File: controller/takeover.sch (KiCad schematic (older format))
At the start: 0 parts

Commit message: Start putting the controller together, add various subsystems
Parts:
- added C1, C10, C11, C12, C13, C14, C16, C2, C3, C4, C5, C6, C8, C9, C? (x2): C, symbol C
- added C15, C7: CP, symbol CP
- added D1, D10, D11, D12, D2, D3, D4, D5, D6, D7, D8, D9, D? (x2): D_ALT, symbol D_ALT
- added J1, J10, J11, J12, J13, J2, J3, J4, J5, J6, J7, J8, J9, J? (x3): CONN_01X02, symbol CONN_01X02
- added K1, K10, K11, K12, K13, K14, K2, K3, K4, K5, K6, K7, K8, K9: RELAY_SEPARATED, symbol RELAY_SEPARATED
- added R1, R2: R, symbol R
- added U1, U2: ULN2003, symbol ULN2003
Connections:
- net labels added: +5V, COMMON_OUT, COMMON_REAL, DIR_SW_BACK_HACK, DIR_SW_BACK_OUT, DIR_SW_BACK_REAL, DIR_SW_FWD_HACK, DIR_SW_FWD_OUT, DIR_SW_FWD_REAL, GAZ_POT_GND_HACK, GAZ_POT_GND_OUT, GAZ_POT_GND_REAL, GAZ_POT_V_HACK, GAZ_POT_V_OUT, GAZ_POT_V_REAL, GAZ_POT_WIPER_HACK, GAZ_POT_WIPER_OUT, GAZ_POT_WIPER_REAL, GAZ_SW_COMMON, GAZ_SW_COMMON_OUT, GAZ_SW_COMMON_REAL, GAZ_SW_NC_HACK, GAZ_SW_NC_OUT, GAZ_SW_NC_REAL, GAZ_SW_NO_HACK, GAZ_SW_NO_OUT, GAZ_SW_NO_REAL, GND, HORN_SW_HACK, HORN_SW_OUT, HORN_SW_REAL, PARKING_HACK, PARKING_OUT, PARKING_REAL, STEERING_COMMON, VCC
- wire segments 0 -> 200
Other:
- note added: "TODO: MIRGALKĖ"
- note added: "TODO: RAKTELIS"
- note added: "TODO: SĖDYNĖ"
- note added: "TODO: ŠVIESOS"

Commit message: Add more stuff to controller, start sourcing parts
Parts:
- removed J1, J10, J11, J12, J13, J2, J3, J4, J5, J6, J7, J8, J9, J? (x3): CONN_01X02, symbol CONN_01X02
- removed U1, U2: ULN2003, symbol ULN2003
- added C19, C32: C, Capacitors_SMD:C_0603_HandSoldering, symbol C
- added D15, D27: D_ALT, Diodes_SMD:D_SOD-123, symbol D_ALT
- added D28, D29: 16V, symbol D_Zener
- added J? (x4): CONN_01X10, Connectors_Terminal_Blocks:TerminalBlock_Pheonix_MKDS1.5-10pol, symbol CONN_01X10
- added K15: RELAY_SEPARATED, smalsiukas-footpints:Relay_SPDT, symbol RELAY_SEPARATED
- added K16: RELAY_SEPARATED, symbol RELAY_SEPARATED
- added U2, U6: ULN2801A, Housings_SOIC:SOIC-18W_7.5x11.6mm_Pitch1.27mm, symbol ULN2801A
- C1, C10, C11, C12, C13, C14, C2, C3, C4, C5, C6, C9: footprint (none) -> Capacitors_SMD:C_0603_HandSoldering; Distributor (none) -> ?; Manufacturer (none) -> ?; PartNo (none) -> ?
- C17, C18: renamed from C?; footprint (none) -> Capacitors_SMD:C_0603_HandSoldering; Distributor (none) -> ?; Manufacturer (none) -> ?; PartNo (none) -> ?
- D1: footprint (none) -> Diodes_SMD:D_SOD-123; Distributor (none) -> 1510679; Manufacturer (none) -> ?; PartNo (none) -> PMEG2020EH
- D10, D11, D12, D2, D3, D4, D5, D6, D7, D8, D9: footprint (none) -> Diodes_SMD:D_SOD-123; Distributor (none) -> ?; Manufacturer (none) -> ?; PartNo (none) -> ?
- D13, D14: renamed from D?; footprint (none) -> Diodes_SMD:D_SOD-123; Distributor (none) -> ?; Manufacturer (none) -> ?; PartNo (none) -> ?
- K1, K10, K11, K12, K13, K14, K2, K3, K4, K5, K6, K7, K8, K9: footprint (none) -> smalsiukas-footpints:Relay_SPDT
- renumbered R1 to R91, R2 to R92
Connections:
- net labels added: AUX_COMMON, AUX_COMMON_OUT, AUX_COMMON_REAL, AUX_HACK, AUX_OUT, AUX_REAL, KEY_COLD_HACK, KEY_COLD_OUT, KEY_COLD_REAL, KEY_HOT_HACK, KEY_HOT_OUT, KEY_HOT_REAL, LIGHTS_COMMON, LIGHTS_COMMON_OUT, LIGHTS_COMMON_REAL, LIGHTS_HACK, LIGHTS_OUT, LIGHTS_REAL, MIRGALKE_HACK, MIRGALKE_OUT, MIRGALKE_REAL, SEAT_GND_HACK, SEAT_GND_OUT, SEAT_GND_REAL, SEAT_HACK, SEAT_OUT, SEAT_REAL, TAKEOVER
- net labels removed: +5V
- wire segments 200 -> 306
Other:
- note removed: "TODO: MIRGALKĖ"
- note removed: "TODO: RAKTELIS"
- note removed: "TODO: SĖDYNĖ"
- note removed: "TODO: ŠVIESOS"
- moved on the sheet: C16, K10A, K10B, K11A, K11B, K12A, K12B, K13A, K13B, K14A, K14B, K7B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

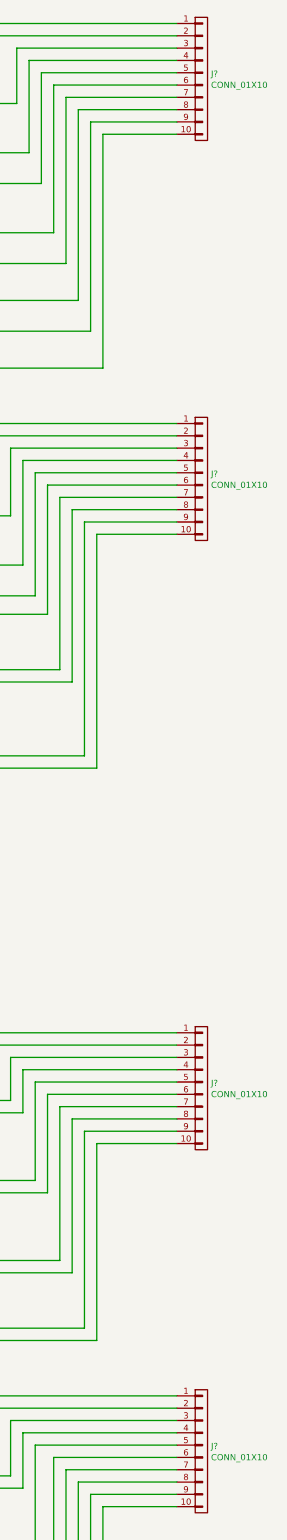
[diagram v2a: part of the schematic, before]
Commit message: Change gas pedal interface so that it supports going up and down from the middle voltage so that it's compatible with Linde forklift gas mechanism
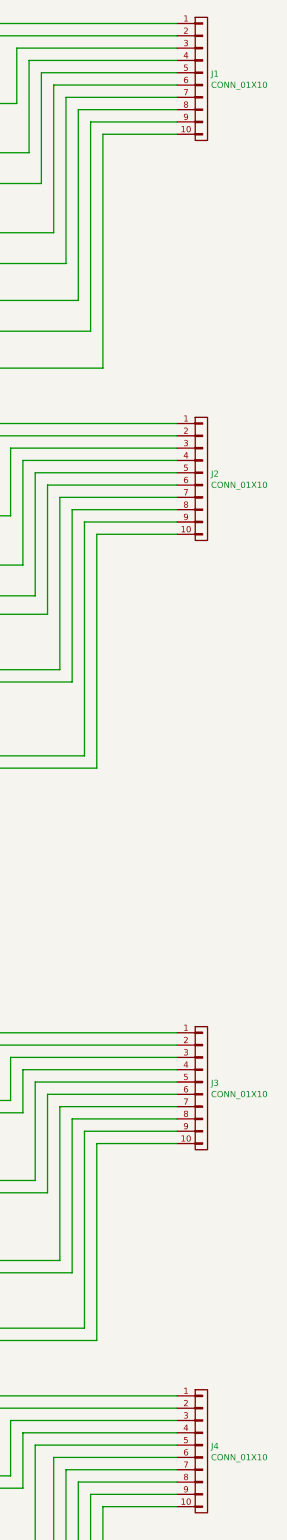
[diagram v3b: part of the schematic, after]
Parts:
- C16: footprint (none) -> Capacitors_SMD:C_0603_HandSoldering
- K1, K10, K11, K12, K13, K14, K15, K16, K2, K3, K4, K5, K6, K7, K8, K9: footprint (none) -> smalsiukas-footpints:Relay_SPDT
- R91, R92: footprint (none) -> Resistors_SMD:R_0603_HandSoldering
- gave numbers to parts that had none: 4
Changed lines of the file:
@@
 F 0 "K2" V 13100 2150 50  0000 C CNN
 F 1 "RELAY_SEPARATED" V 13537 2150 50  0001 C CNN
-F 2 "" H 8700 -250 50  0000 C CNN
+F 2 "smalsiukas-footpints:Relay_SPDT" H 8700 -250 50  0001 C CNN
 F 3 "" H 8700 -250 50  0000 C CNN
 F 4 "?" H 13350 2150 60  0001 C CNN "PartNo"
@@
 F 0 "K9" V 13100 9650 50  0000 C CNN
 F 1 "RELAY_SEPARATED" V 13200 9600 50  0001 C CNN
-F 2 "" H 8700 7200 50  0000 C CNN
+F 2 "smalsiukas-footpints:Relay_SPDT" H 8700 7200 50  0001 C CNN
 F 3 "" H 8700 7200 50  0000 C CNN
 F 4 "?" H 13350 9600 60  0001 C CNN "PartNo"
@@
 F 0 "K3" V 13150 2800 50  0000 C CNN
 F 1 "RELAY_SEPARATED" V 13537 2800 50  0001 C CNN
-F 2 "" H 8700 400 50  0000 C CNN
+F 2 "smalsiukas-footpints:Relay_SPDT" H 8700 400 50  0001 C CNN
 F 3 "" H 8700 400 50  0000 C CNN
 F 4 "?" H 13350 2800 60  0001 C CNN "PartNo"
@@
 F 0 "K10" V 13150 10250 50  0000 C CNN
 F 1 "RELAY_SEPARATED" V 13150 10250 50  0001 C CNN
-F 2 "" H 8700 7850 50  0000 C CNN
+F 2 "smalsiukas-footpints:Relay_SPDT" H 8700 7850 50  0001 C CNN
 F 3 "" H 8700 7850 50  0000 C CNN
 F 4 "?" H 13350 10250 60  0001 C CNN "PartNo"
@@
 F 0 "K1" V 13150 1500 50  0000 C CNN
 F 1 "RELAY_SEPARATED" V 13116 1500 50  0001 C CNN
-F 2 "" H 8700 -900 50  0000 C CNN
+F 2 "smalsiukas-footpints:Relay_SPDT" H 8700 -900 50  0001 C CNN
 F 3 "" H 8700 -900 50  0000 C CNN
 F 4 "?" H 13350 1500 60  0001 C CNN "PartNo"
@@
 F 0 "K8" V 13025 6800 50  0000 C CNN
 F 1 "RELAY_SEPARATED" V 13116 6800 50  0001 C CNN
-F 2 "" H 8700 4400 50  0000 C CNN
+F 2 "smalsiukas-footpints:Relay_SPDT" H 8700 4400 50  0001 C CNN
 F 3 "" H 8700 4400 50  0000 C CNN
 F 4 "?" H 13350 6800 60  0001 C CNN "PartNo"
@@
 $EndComp
 $Comp
-L GND #PWR01
+L GND #PWR1
 U 1 1 58C02975
 P 2100 3850
-F 0 "#PWR01" H -2250 300 50  0001 C CNN
+F 0 "#PWR1" H -2250 300 50  0001 C CNN
 F 1 "GND" H 2105 3677 50  0000 C CNN
 F 2 "" H -2250 550 50  0001 C CNN
@@
 F 0 "R91" H 1569 3746 50  0000 L CNN
 F 1 "R" H 1569 3655 50  0000 L CNN
-F 2 "" V -2120 1200 50  0001 C CNN
+F 2 "Resistors_SMD:R_0603_HandSoldering" V -2120 1200 50  0001 C CNN
 F 3 "" H -2050 1200 50  0001 C CNN
 	1    1500 3700
@@
 $EndComp
 $Comp
-L GND #PWR02
+L GND #PWR2
 U 1 1 58C02979
 P 4400 2700
-F 0 "#PWR02" H 50  -850 50  0001 C CNN
+F 0 "#PWR2" H 50  -850 50  0001 C CNN
 F 1 "GND" H 4405 2527 50  0000 C CNN
 F 2 "" H 50  -600 50  0001 C CNN
@@
 F 0 "K5" V 13550 4100 50  0000 C CNN
 F 1 "RELAY_SEPARATED" V 13537 4100 50  0001 C CNN
-F 2 "" H 8700 1700 50  0000 C CNN
+F 2 "smalsiukas-footpints:Relay_SPDT" H 8700 1700 50  0001 C CNN
 F 3 "" H 8700 1700 50  0000 C CNN
 F 4 "?" H 13350 4100 60  0001 C CNN "PartNo"
@@
 F 0 "K12" V 13150 11450 50  0000 C CNN
 F 1 "RELAY_SEPARATED" V 13200 11450 50  0001 C CNN
-F 2 "" H 8700 9050 50  0000 C CNN
+F 2 "smalsiukas-footpints:Relay_SPDT" H 8700 9050 50  0001 C CNN
 F 3 "" H 8700 9050 50  0000 C CNN
 F 4 "?" H 13350 11450 60  0001 C CNN "PartNo"
@@
 F 0 "K6" V 13150 4850 50  0000 C CNN
 F 1 "RELAY_SEPARATED" V 13537 4850 50  0001 C CNN
-F 2 "" H 8700 2450 50  0000 C CNN
+F 2 "smalsiukas-footpints:Relay_SPDT" H 8700 2450 50  0001 C CNN
 F 3 "" H 8700 2450 50  0000 C CNN
 F 4 "?" H 13350 4850 60  0001 C CNN "PartNo"
@@
 F 0 "K13" V 13050 12000 50  0000 C CNN
 F 1 "RELAY_SEPARATED" V 13150 12000 50  0001 C CNN
-F 2 "" H 8700 9600 50  0000 C CNN
+F 2 "smalsiukas-footpints:Relay_SPDT" H 8700 9600 50  0001 C CNN
 F 3 "" H 8700 9600 50  0000 C CNN
 F 4 "?" H 13350 12000 60  0001 C CNN "PartNo"
@@
 F 0 "K4" V 13150 3350 50  0000 C CNN
 F 1 "RELAY_SEPARATED" V 13116 3350 50  0001 C CNN
-F 2 "" H 8700 950 50  0000 C CNN
+F 2 "smalsiukas-footpints:Relay_SPDT" H 8700 950 50  0001 C CNN
 F 3 "" H 8700 950 50  0000 C CNN
 F 4 "?" H 13350 3350 60  0001 C CNN "PartNo"
@@
 F 0 "K11" V 13150 10900 50  0000 C CNN
 F 1 "RELAY_SEPARATED" V 13116 10900 50  0001 C CNN
-F 2 "" H 8700 8500 50  0000 C CNN
+F 2 "smalsiukas-footpints:Relay_SPDT" H 8700 8500 50  0001 C CNN
 F 3 "" H 8700 8500 50  0000 C CNN
 F 4 "?" H 13350 10900 60  0001 C CNN "PartNo"
@@
 $EndComp
 $Comp
-L GND #PWR03
+L GND #PWR4
 U 1 1 58C03628
 P 6550 3750
-F 0 "#PWR03" H 2200 200 50  0001 C CNN
+F 0 "#PWR4" H 2200 200 50  0001 C CNN
 F 1 "GND" H 6555 3577 50  0000 C CNN
 F 2 "" H 2200 450 50  0001 C CNN
@@
 F 0 "R92" H 6019 3646 50  0000 L CNN
 F 1 "R" H 6019 3555 50  0000 L CNN
-F 2 "" V 2330 1100 50  0001 C CNN
+F 2 "Resistors_SMD:R_0603_HandSoldering" V 2330 1100 50  0001 C CNN
 F 3 "" H 2400 1100 50  0001 C CNN
 	1    5950 3600
@@
 $EndComp
 $Comp
-L GND #PWR04
+L GND #PWR5
 U 1 1 58C0362C
 P 8850 2600
-F 0 "#PWR04" H 4500 -950 50  0001 C CNN
+F 0 "#PWR5" H 4500 -950 50  0001 C CNN
 F 1 "GND" H 8855 2427 50  0000 C CNN
 F 2 "" H 4500 -700 50  0001 C CNN
@@
 F 0 "C16" H 9085 2404 50  0000 R CNN
 F 1 "C" H 9085 2495 50  0000 R CNN
-F 2 "" H 1088 -3400 50  0001 C CNN
+F 2 "Capacitors_SMD:C_0603_HandSoldering" H 1088 -3400 50  0001 C CNN
 F 3 "" H 1050 -3250 50  0001 C CNN
 	1    9200 2450
@@
 F 0 "K7" V 13150 6100 50  0000 C CNN
 F 1 "RELAY_SEPARATED" V 13537 6100 50  0001 C CNN
-F 2 "" H 8700 3700 50  0000 C CNN
+F 2 "smalsiukas-footpints:Relay_SPDT" H 8700 3700 50  0001 C CNN
 F 3 "" H 8700 3700 50  0000 C CNN
 F 4 "?" H 13350 6100 60  0001 C CNN "PartNo"
@@
 F 0 "K14" V 13050 12650 50  0000 C CNN
 F 1 "RELAY_SEPARATED" V 13150 12650 50  0000 C CNN
-F 2 "" H 8700 10250 50  0000 C CNN
+F 2 "smalsiukas-footpints:Relay_SPDT" H 8700 10250 50  0001 C CNN
 F 3 "" H 8700 10250 50  0000 C CNN
 F 4 "?" H 13350 12650 60  0001 C CNN "PartNo"
@@
 F 0 "K16" V 13100 14150 50  0000 C CNN
 F 1 "RELAY_SEPARATED" V 13487 14150 50  0001 C CNN
-F 2 "" H 8650 11750 50  0000 C CNN
+F 2 "smalsiukas-footpints:Relay_SPDT" H 8650 11750 50  0001 C CNN
 F 3 "" H 8650 11750 50  0000 C CNN
 F 4 "?" H 13300 14150 60  0001 C CNN "PartNo"
@@
 F 0 "K15" V 13050 13400 50  0000 C CNN
 F 1 "RELAY_SEPARATED" V 13150 13400 50  0000 C CNN
-F 2 "" H 8700 11000 50  0000 C CNN
+F 2 "smalsiukas-footpints:Relay_SPDT" H 8700 11000 50  0001 C CNN
 F 3 "" H 8700 11000 50  0000 C CNN
 F 4 "?" H 13350 13400 60  0001 C CNN "PartNo"
@@
 $EndComp
 $Comp
-L GND #PWR05
+L GND #PWR3
 U 1 1 58D4FA8B
 P 5150 2700
-F 0 "#PWR05" H 800 -850 50  0001 C CNN
+F 0 "#PWR3" H 800 -850 50  0001 C CNN
 F 1 "GND" H 5155 2527 50  0000 C CNN
 F 2 "" H 800 -600 50  0001 C CNN
@@
 $EndComp
 $Comp
-L GND #PWR06
+L GND #PWR6
 U 1 1 58D50C69
 P 9550 2600
-F 0 "#PWR06" H 5200 -950 50  0001 C CNN
+F 0 "#PWR6" H 5200 -950 50  0001 C CNN
 F 1 "GND" H 9555 2427 50  0000 C CNN
 F 2 "" H 5200 -700 50  0001 C CNN
@@
 $EndComp
 $Comp
-L CONN_01X10 J?
+L CONN_01X10 J1
 U 1 1 58C69E7E
 P 16350 1300
-F 0 "J?" H 16428 1341 50  0000 L CNN
+F 0 "J1" H 16428 1341 50  0000 L CNN
 F 1 "CONN_01X10" H 16428 1250 50  0000 L CNN
 F 2 "Connectors_Terminal_Blocks:TerminalBlock_Pheonix_MKDS1.5-10pol" H -3750 -200 50  0001 C CNN
@@
 $EndComp
 $Comp
-L CONN_01X10 J?
+L CONN_01X10 J2
 U 1 1 58C75771
 P 16350 4550
-F 0 "J?" H 16428 4591 50  0000 L CNN
+F 0 "J2" H 16428 4591 50  0000 L CNN
 F 1 "CONN_01X10" H 16428 4500 50  0000 L CNN
 F 2 "Connectors_Terminal_Blocks:TerminalBlock_Pheonix_MKDS1.5-10pol" H -3750 3050 50  0001 C CNN
@@
 $EndComp
 $Comp
-L CONN_01X10 J?
+L CONN_01X10 J3
 U 1 1 58C75B19
 P 16350 9500
-F 0 "J?" H 16428 9541 50  0000 L CNN
+F 0 "J3" H 16428 9541 50  0000 L CNN
 F 1 "CONN_01X10" H 16428 9450 50  0000 L CNN
 F 2 "Connectors_Terminal_Blocks:TerminalBlock_Pheonix_MKDS1.5-10pol" H -3750 8000 50  0001 C CNN
@@
 $EndComp
 $Comp
-L CONN_01X10 J?
+L CONN_01X10 J4
 U 1 1 58C76546
 P 16350 12450
-F 0 "J?" H 16428 12491 50  0000 L CNN
+F 0 "J4" H 16428 12491 50  0000 L CNN
 F 1 "CONN_01X10" H 16428 12400 50  0000 L CNN
 F 2 "Connectors_Terminal_Blocks:TerminalBlock_Pheonix_MKDS1.5-10pol" H -3750 10950 50  0001 C CNN

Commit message: More or less final controller board
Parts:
- removed C15, C7: CP, symbol CP
- added C15, C7: 470u, Capacitors_ThroughHole:CP_Radial_D16.0mm_P7.50mm, symbol CP1
- C16: footprint Capacitors_SMD:C_0603_HandSoldering -> Capacitors_SMD:C_1210_HandSoldering; Distributor (none) -> ?; Manufacturer (none) -> ?; PartNo (none) -> ?
- C8: footprint (none) -> Capacitors_SMD:C_1210_HandSoldering; Distributor (none) -> ?; Manufacturer (none) -> ?; PartNo (none) -> ?
- D28, D29: footprint (none) -> Diodes_SMD:D_SMB_Handsoldering; Distributor (none) -> 1431172; Manufacturer (none) -> ON SEMI; PartNo (none) -> 1SMB5930BT3G
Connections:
- net GND: now also C15.2, C7.2
- net VCC: now also C15.1, C7.1
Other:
- note added: "Relės: HFD23/012-1ZS @ TME.eu\nhttp://www.tme.eu/en/details/hfd23_012-1zs/miniature-electromagnetic-relays/hongfa-relay/"
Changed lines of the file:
@@
 LIBS:valves
 LIBS:mic-parts
+LIBS:shield_arduino
 LIBS:controller-cache
 EELAYER 26 0
@@
 $EndComp
 $Comp
-L GND #PWR1
+L GND #PWR03
 U 1 1 58C02975
 P 2100 3850
-F 0 "#PWR1" H -2250 300 50  0001 C CNN
+F 0 "#PWR03" H -2250 300 50  0001 C CNN
 F 1 "GND" H 2105 3677 50  0000 C CNN
 F 2 "" H -2250 550 50  0001 C CNN
@@
 $EndComp
 $Comp
-L CP C7
-U 1 1 58C02978
-P 4400 2550
-F 0 "C7" H 4518 2596 50  0000 L CNN
-F 1 "CP" H 4518 2505 50  0000 L CNN
-F 2 "" H -2662 750 50  0001 C CNN
-F 3 "" H -2700 900 50  0001 C CNN
-	1    4400 2550
-	1    0    0    -1
-$EndComp
-$Comp
-L GND #PWR2
+L GND #PWR04
 U 1 1 58C02979
 P 4400 2700
-F 0 "#PWR2" H 50  -850 50  0001 C CNN
+F 0 "#PWR04" H 50  -850 50  0001 C CNN
 F 1 "GND" H 4405 2527 50  0000 C CNN
 F 2 "" H 50  -600 50  0001 C CNN
@@
 F 0 "C8" H 4635 2504 50  0000 R CNN
 F 1 "C" H 4635 2595 50  0000 R CNN
-F 2 "" H -3362 -3300 50  0001 C CNN
+F 2 "Capacitors_SMD:C_1210_HandSoldering" H -3362 -3300 50  0001 C CNN
 F 3 "" H -3400 -3150 50  0001 C CNN
+F 4 "?" H 4750 2550 60  0001 C CNN "PartNo"
+F 5 "?" H 4750 2550 60  0001 C CNN "Manufacturer"
+F 6 "?" H 4750 2550 60  0001 C CNN "Distributor"
 	1    4750 2550
 	-1   0    0    1
@@
 $EndComp
 $Comp
-L GND #PWR4
+L GND #PWR05
 U 1 1 58C03628
 P 6550 3750
-F 0 "#PWR4" H 2200 200 50  0001 C CNN
+F 0 "#PWR05" H 2200 200 50  0001 C CNN
 F 1 "GND" H 6555 3577 50  0000 C CNN
 F 2 "" H 2200 450 50  0001 C CNN
@@
 $EndComp
 $Comp
-L CP C15
-U 1 1 58C0362B
-P 8850 2450
-F 0 "C15" H 8968 2496 50  0000 L CNN
-F 1 "CP" H 8968 2405 50  0000 L CNN
-F 2 "" H 1788 650 50  0001 C CNN
-F 3 "" H 1750 800 50  0001 C CNN
-	1    8850 2450
-	1    0    0    -1
-$EndComp
-$Comp
-L GND #PWR5
+L GND #PWR06
 U 1 1 58C0362C
 P 8850 2600
-F 0 "#PWR5" H 4500 -950 50  0001 C CNN
+F 0 "#PWR06" H 4500 -950 50  0001 C CNN
 F 1 "GND" H 8855 2427 50  0000 C CNN
 F 2 "" H 4500 -700 50  0001 C CNN
@@
 F 0 "C16" H 9085 2404 50  0000 R CNN
 F 1 "C" H 9085 2495 50  0000 R CNN
-F 2 "Capacitors_SMD:C_0603_HandSoldering" H 1088 -3400 50  0001 C CNN
+F 2 "Capacitors_SMD:C_1210_HandSoldering" H 1088 -3400 50  0001 C CNN
 F 3 "" H 1050 -3250 50  0001 C CNN
+F 4 "?" H 9200 2450 60  0001 C CNN "PartNo"
+F 5 "?" H 9200 2450 60  0001 C CNN "Manufacturer"
+F 6 "?" H 9200 2450 60  0001 C CNN "Distributor"
 	1    9200 2450
 	-1   0    0    1
@@
 TAKEOVER
 $Comp
-L D_Zener D28
-U 1 1 58D4F74C
-P 5150 2550
-F 0 "D28" V 5104 2629 50  0000 L CNN
-F 1 "16V" V 5195 2629 50  0000 L CNN
-F 2 "" H -350 500 50  0001 C CNN
-F 3 "" H -350 500 50  0001 C CNN
-	1    5150 2550
-	0    1    1    0
-$EndComp
-$Comp
-L GND #PWR3
+L GND #PWR07
 U 1 1 58D4FA8B
 P 5150 2700
-F 0 "#PWR3" H 800 -850 50  0001 C CNN
+F 0 "#PWR07" H 800 -850 50  0001 C CNN
 F 1 "GND" H 5155 2527 50  0000 C CNN
 F 2 "" H 800 -600 50  0001 C CNN
@@
 $EndComp
 $Comp
-L D_Zener D29
-U 1 1 58D50C63
-P 9550 2450
-F 0 "D29" V 9504 2529 50  0000 L CNN
-F 1 "16V" V 9595 2529 50  0000 L CNN
-F 2 "" H 4050 400 50  0001 C CNN
-F 3 "" H 4050 400 50  0001 C CNN
-	1    9550 2450
-	0    1    1    0
-$EndComp
-$Comp
-L GND #PWR6
+L GND #PWR08
 U 1 1 58D50C69
 P 9550 2600
-F 0 "#PWR6" H 5200 -950 50  0001 C CNN
+F 0 "#PWR08" H 5200 -950 50  0001 C CNN
 F 1 "GND" H 9555 2427 50  0000 C CNN
 F 2 "" H 5200 -700 50  0001 C CNN
@@
 Wire Wire Line
 	15550 14950 14650 14950
+$Comp
+L D_Zener D29
+U 1 1 58C9A510
+P 9550 2450
+F 0 "D29" V 9504 2529 50  0000 L CNN
+F 1 "16V" V 9595 2529 50  0000 L CNN
+F 2 "Diodes_SMD:D_SMB_Handsoldering" H 4250 850 50  0001 C CNN
+F 3 "" H 4250 850 50  0001 C CNN
+F 4 "1SMB5930BT3G" H 9550 2450 60  0001 C CNN "PartNo"
+F 5 "ON SEMI" H 9550 2450 60  0001 C CNN "Manufacturer"
+F 6 "1431172" H 9550 2450 60  0001 C CNN "Distributor"
+	1    9550 2450
+	0    1    1    0
+$EndComp
+$Comp
+L D_Zener D28
+U 1 1 58C9A6C8
+P 5150 2550
+F 0 "D28" V 5104 2629 50  0000 L CNN
+F 1 "16V" V 5195 2629 50  0000 L CNN
+F 2 "Diodes_SMD:D_SMB_Handsoldering" H -150 950 50  0001 C CNN
+F 3 "" H -150 950 50  0001 C CNN
+F 4 "1SMB5930BT3G" H 5150 2550 60  0001 C CNN "PartNo"
+F 5 "ON SEMI" H 5150 2550 60  0001 C CNN "Manufacturer"
+F 6 "1431172" H 5150 2550 60  0001 C CNN "Distributor"
+	1    5150 2550
+	0    1    1    0
+$EndComp
+$Comp
+L CP1 C15
+U 1 1 58CA0DBC
+P 8850 2450
+F 0 "C15" H 8965 2496 50  0000 L CNN
+F 1 "470u" H 8965 2405 50  0000 L CNN
+F 2 "Capacitors_ThroughHole:CP_Radial_D16.0mm_P7.50mm" H 3700 700 50  0001 C CNN
+F 3 "" H 3700 700 50  0001 C CNN
+F 4 "ECA2AAM471X" H 8850 2450 60  0001 C CNN "PartNo"
+F 5 "PANASONIC" H 8850 2450 60  0001 C CNN "Manufacturer"
+F 6 "8767696" H 8850 2450 60  0001 C CNN "Distributor"
+	1    8850 2450
+	-1   0    0    -1
+$EndComp
+$Comp
+L CP1 C7
+U 1 1 58CA1064
+P 4400 2550
+F 0 "C7" H 4515 2596 50  0000 L CNN
+F 1 "470u" H 4515 2505 50  0000 L CNN
+F 2 "Capacitors_ThroughHole:CP_Radial_D16.0mm_P7.50mm" H -750 800 50  0001 C CNN
+F 3 "" H -750 800 50  0001 C CNN
+F 4 "ECA2AAM471X" H 4400 2550 60  0001 C CNN "PartNo"
+F 5 "PANASONIC" H 4400 2550 60  0001 C CNN "Manufacturer"
+F 6 "8767696" H 4400 2550 60  0001 C CNN "Distributor"
+	1    4400 2550
+	-1   0    0    -1
+$EndComp
+Text Notes 3150 1650 0    60   ~ 0
+Relės: HFD23/012-1ZS @ TME.eu\nhttp://www.tme.eu/en/details/hfd23_012-1zs/miniature-electromagnetic-relays/hongfa-relay/
 $EndSCHEMATC

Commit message: Some progress with controller board routing
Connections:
- net AUX_COMMON: now also J3.1 (P1), J3.2 (P2); no longer J4.10 (P10), J4.9 (P9)
- net AUX_HACK: now also K13.4; no longer K16.4
- net AUX_OUT: now also J3.3 (P3), K13.3; no longer J4.7 (P7), K16.3
- net AUX_REAL: now also J3.4 (P4), K13.2; no longer J4.8 (P8), K16.2
- net GAZ_POT_GND_OUT: now also J4.9 (P9); no longer J3.9 (P9)
- net GAZ_POT_GND_REAL: now also J4.10 (P10); no longer J3.10 (P10)
- net GAZ_POT_V_OUT: now also J4.7 (P7); no longer J3.7 (P7)
- net GAZ_POT_V_REAL: now also J4.8 (P8); no longer J3.8 (P8)
- net GAZ_POT_WIPER_HACK: now also K16.4; no longer K13.4
- net GAZ_POT_WIPER_OUT: now also J3.9 (P9), K16.3; no longer J4.1 (P1), K13.3
- net GAZ_POT_WIPER_REAL: now also J3.10 (P10), K16.2; no longer J4.2 (P2), K13.2
- net GAZ_SW_COMMON: now also J4.1 (P1), J4.2 (P2); no longer J3.1 (P1), J3.2 (P2)
- net GAZ_SW_NC_OUT: now also J4.3 (P3); no longer J3.3 (P3)
- net GAZ_SW_NC_REAL: now also J4.4 (P4); no longer J3.4 (P4)
- net GAZ_SW_NO_OUT: now also J4.5 (P5); no longer J3.5 (P5)
- net GAZ_SW_NO_REAL: now also J4.6 (P6); no longer J3.6 (P6)
- net KEY_COLD_HACK: now also K15.4; no longer K6.4
- net KEY_COLD_OUT: now also J3.7 (P7), K15.3; no longer J2.3 (P3), K6.3
- net KEY_COLD_REAL: now also J3.8 (P8), K15.2; no longer J2.4 (P4), K6.2
- net KEY_HOT_HACK: now also K14.4; no longer K5.4
- net KEY_HOT_OUT: now also J3.5 (P5), K14.3; no longer J2.1 (P1), K5.3
- net KEY_HOT_REAL: now also J3.6 (P6), K14.2; no longer J2.2 (P2), K5.2
- net SEAT_GND_HACK: now also K5.4; no longer K14.4
- net SEAT_GND_OUT: now also J2.1 (P1), K5.3; no longer J4.3 (P3), K14.3
- net SEAT_GND_REAL: now also J2.2 (P2), K5.2; no longer J4.4 (P4), K14.2
- net SEAT_HACK: now also K6.4; no longer K15.4
- net SEAT_OUT: now also J2.3 (P3), K6.3; no longer J4.5 (P5), K15.3
- net SEAT_REAL: now also J2.4 (P4), K6.2; no longer J4.6 (P6), K15.2
- net at C1.2, D1.2 (A), K1.10: now also U6.11 (O8); no longer U6.18 (O1)
- net at C3.2, D3.2 (A), K3.10: now also U6.13 (O6); no longer U6.16 (O3)
- net at C10.2, D8.2 (A), K10.10: now also U2.12 (O7); no longer U2.17 (O2)
- net at C32.2, D27.2 (A), K8.10: now also U6.18 (O1); no longer U6.11 (O8)
- net at C2.2, D2.2 (A), K2.10: now also U6.12 (O7); no longer U6.17 (O2)
- net at C9.2, D7.2 (A), K9.10: now also U2.11 (O8); no longer U2.18 (O1)
- net at C6.2, D6.2 (A), K6.10: now also U6.16 (O3); no longer U6.13 (O6)
- net at C5.2, D5.2 (A), K5.10: now also U6.15 (O4); no longer U6.14 (O5)
- net at C4.2, D4.2 (A), K4.10: now also U6.14 (O5); no longer U6.15 (O4)
- net at C13.2, D11.2 (A), K13.10: now also U2.15 (O4); no longer U2.14 (O5)
- net at C11.2, D9.2 (A), K11.10: now also U2.13 (O6); no longer U2.16 (O3)
- net at C12.2, D10.2 (A), K12.10: now also U2.14 (O5); no longer U2.15 (O4)
- net at C14.2, D12.2 (A), K14.10: now also U2.16 (O3); no longer U2.13 (O6)
- net at C17.2, D13.2 (A), K7.10: now also U6.17 (O2); no longer U6.12 (O7)
- net at C18.2, D14.2 (A), K15.10: now also U2.17 (O2); no longer U2.12 (O7)
- net at C19.2, D15.2 (A), K16.1: now also U2.18 (O1); no longer U2.11 (O8)
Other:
- moved on the sheet: J3, J4, K13B, K14B, K15B, K16B, U2, U6
